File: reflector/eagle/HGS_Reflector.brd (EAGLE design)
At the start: 100 x 100 mm, 24 parts, among them J1 U.FL, U3 LP2985XX-N

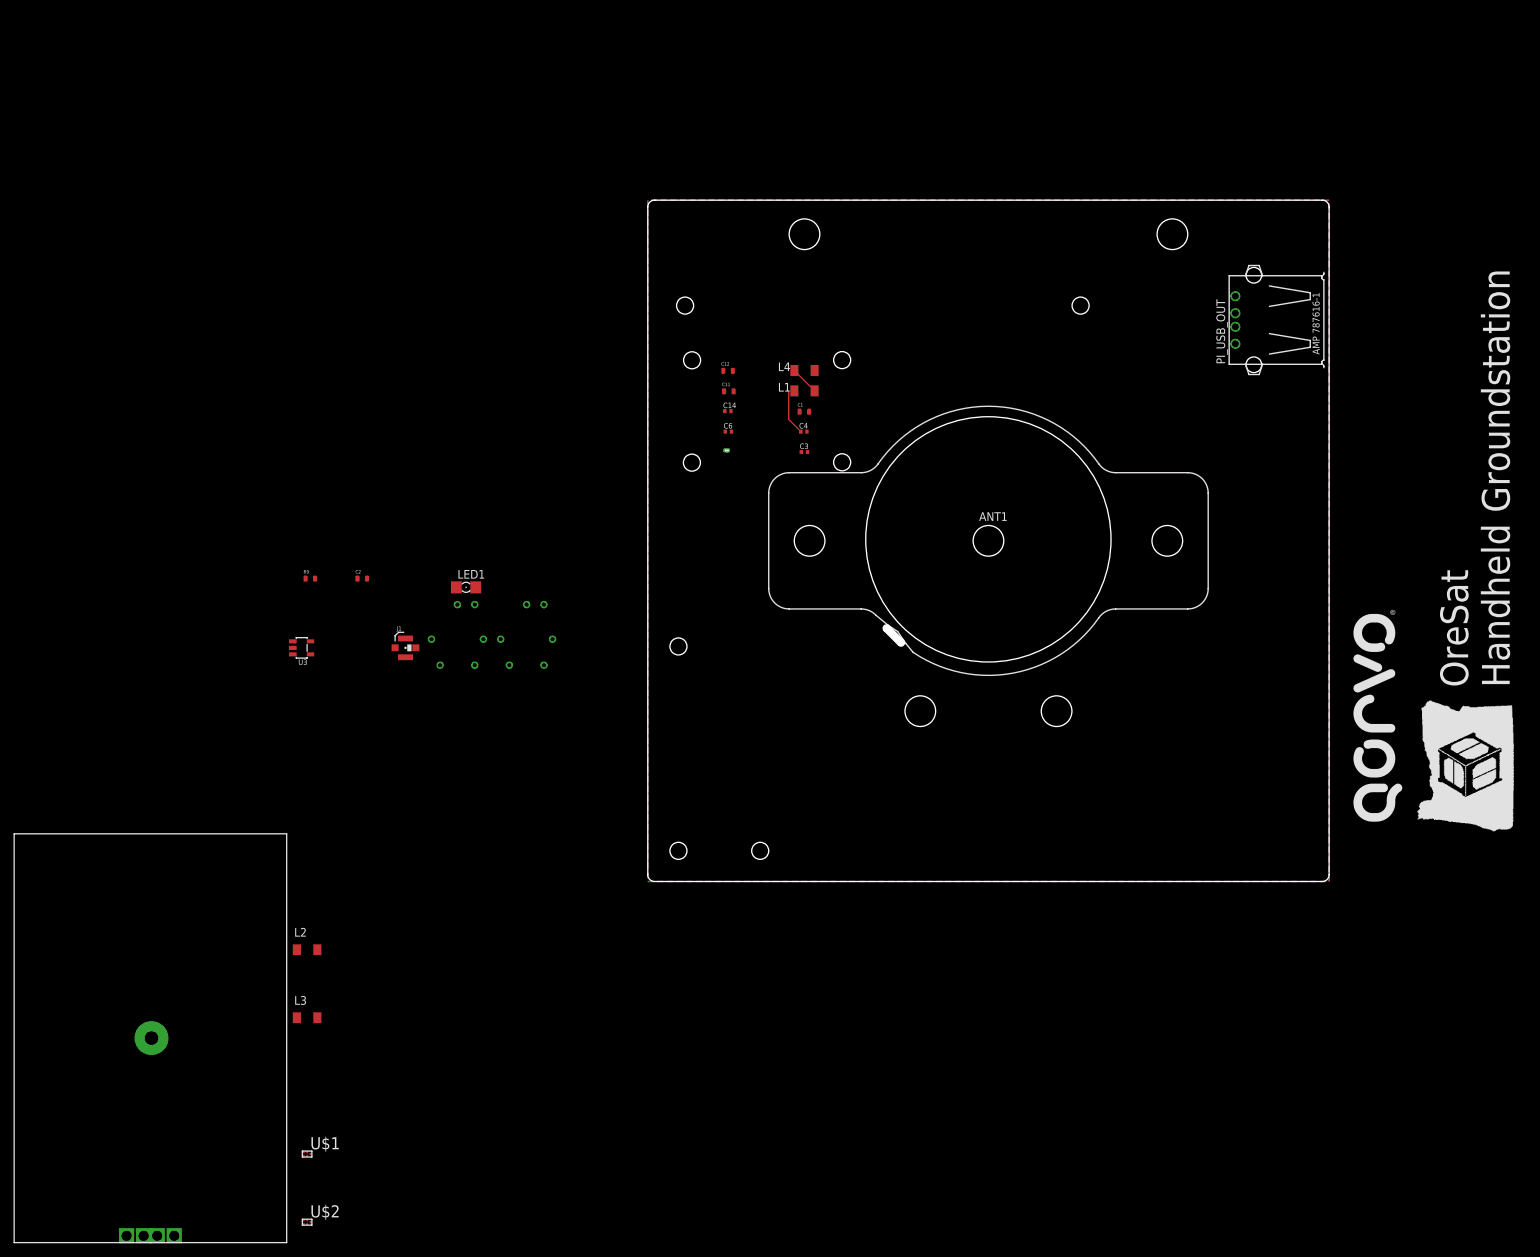
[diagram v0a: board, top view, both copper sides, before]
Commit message: I completed the physical layout of the board for HGS. Currently, I just need to sort through some DRC errors that I don't know how to fix, and do a design review.
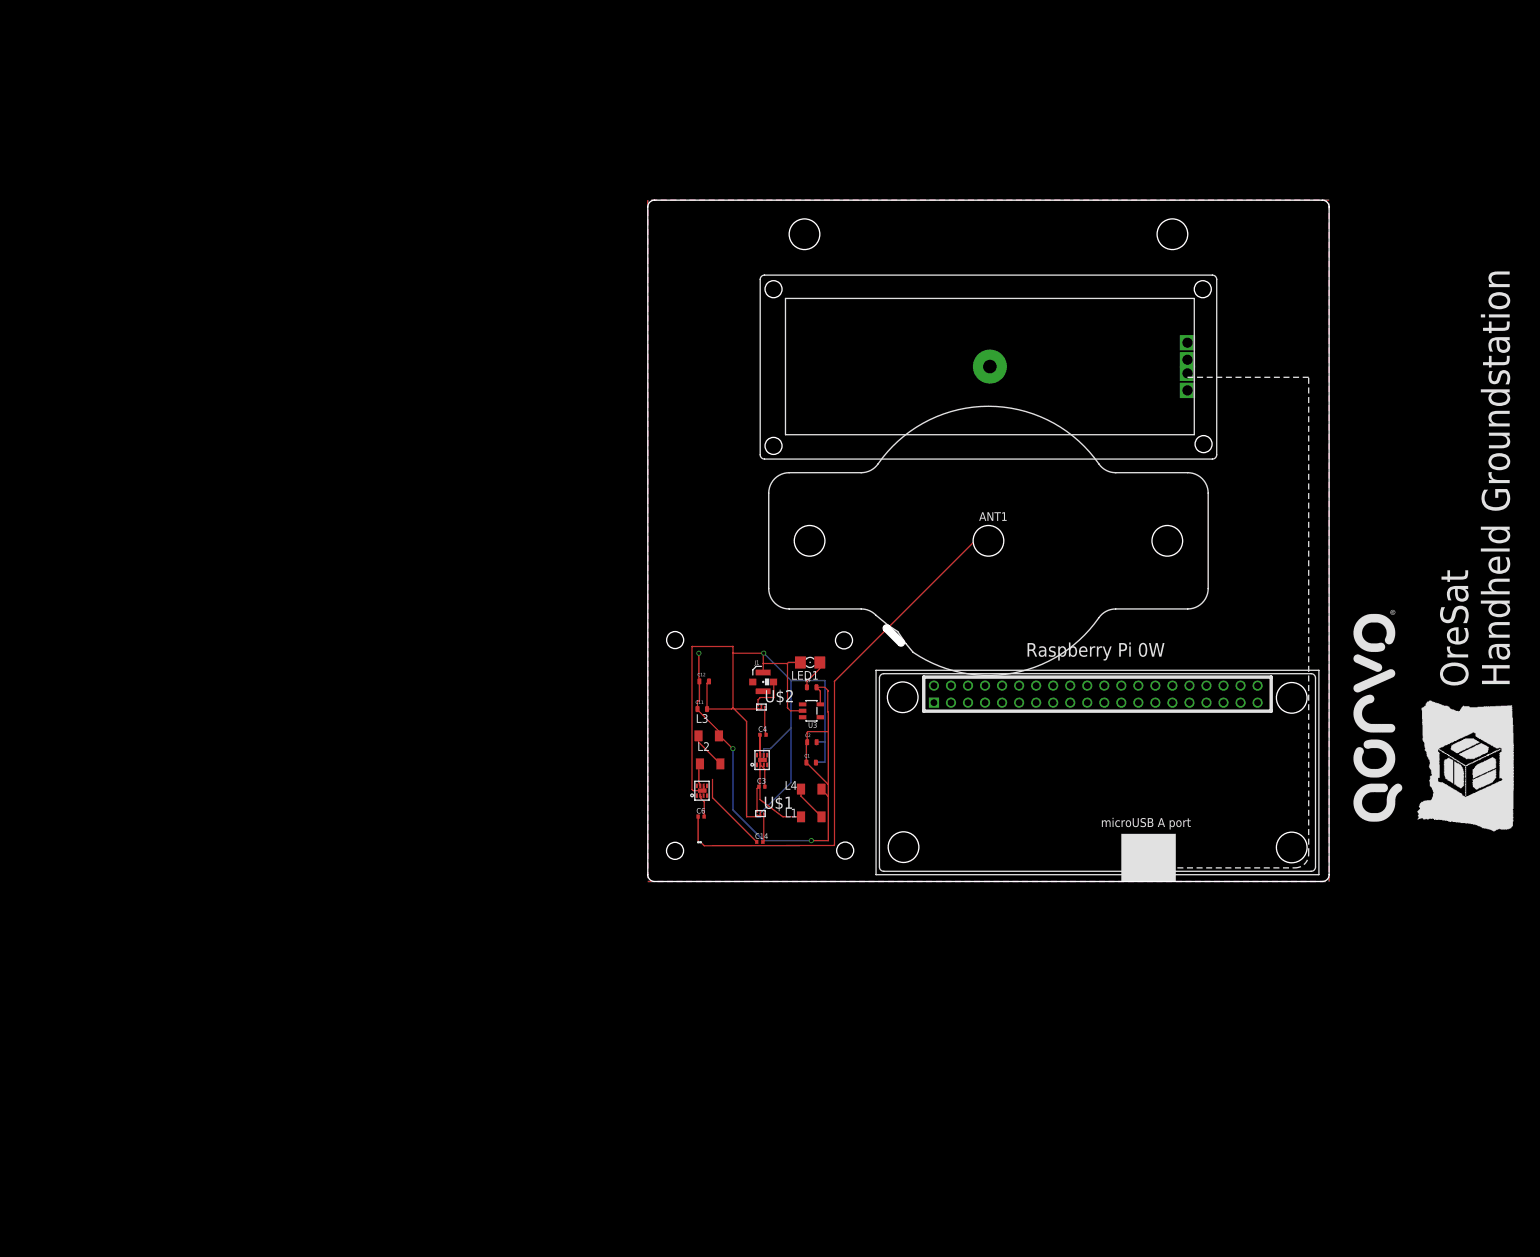
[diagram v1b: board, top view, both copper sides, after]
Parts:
- removed PI_USB_OUT: (no value), con-amp:USB
- added U$5: (no value), Rasp_Pi_0W:RASP_PI_0W
- U$6, U$7: device HGS_Data_Parts:TP3M9037 -> TP3M9037_LNA:TP3M9037
- moved U$4 157.8 mm to (50.2, 75.6), turned to 90 degrees
- moved U$2 100.8 mm to (16.7, 25.6)
- moved U$1 83.2 mm to (16.5, 9.97)
- moved U3 75.4 mm to (24.0, 25.1)
- moved R9 75.3 mm to (24.1, 28.5)
- moved L3 72.0 mm to (8.94, 21.4)
- moved C2 70.2 mm to (24.1, 20.4)
- moved L2 65.1 mm to (9.16, 17.3)
- moved C14 63.4 mm to (16.4, 5.81)
- moved L1 62.5 mm to (24.0, 9.50)
- moved L4 61.5 mm to (24.0, 13.6)
- moved U$3 57.6 mm to (7.59, 5.76), turned to 180 degrees
- moved C6 56.6 mm to (7.83, 9.53)
- moved J1 52.7 mm to (16.9, 29.3)
- moved LED1 51.7 mm to (23.8, 32.2), turned to 180 degrees
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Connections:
- removed net 3.3V1: L4.2
- removed net N$2: C4.1, U$6.RF_OUT
- net 1: no longer PI_USB_OUT.1
- net 3.3V: now also L4.2
- net GND: now also U$6.2X2_DFN_8PIN6, U$6.P$1, U$7.2X2_DFN_8PIN6, U$7.P$1; no longer U$6.GND, U$6.J7, U$6.SHTDN, U$6.VDD, U$7.GND, U$7.J7, U$7.SHTDN, U$7.VDD
- net N$11: now also U$7.2X2_DFN_8PIN2; no longer U$7.RF_IN
- net N$13: now also C4.1, U$6.2X2_DFN_8PIN7
- net N$16: now also U$7.2X2_DFN_8PIN7; no longer U$7.RF_OUT
- net N$18: no longer PI_USB_OUT.2
- net N$19: no longer PI_USB_OUT.3
- net N$8: now also U$6.2X2_DFN_8PIN2; no longer U$6.RF_IN
- net VCC: no longer PI_USB_OUT.4
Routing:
- net GND: track 0.00 -> 146.3 mm, vias 0 -> 1
- net 3.3V: track 0.00 -> 81.6 mm, vias 0 -> 3
- net N$12: track 0.00 -> 74.9 mm
- net N$13: track 0.00 -> 19.4 mm
- net N$16: track 0.00 -> 15.0 mm
- net N$2: track 6.71 -> 0.00 mm
- net N$5: track 0.00 -> 5.54 mm
- net N$7: track 0.00 -> 5.45 mm
- net N$10: track 0.00 -> 4.64 mm
- net N$6: track 0.00 -> 4.22 mm
- net N$3: track 0.00 -> 4.10 mm
- net N$9: track 0.00 -> 3.80 mm
- net N$4: track 0.00 -> 3.75 mm
- net N$8: track 0.00 -> 3.46 mm
- net N$11: track 0.00 -> 3.32 mm
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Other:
- board text removed: "Raspberry Pi Zero area"

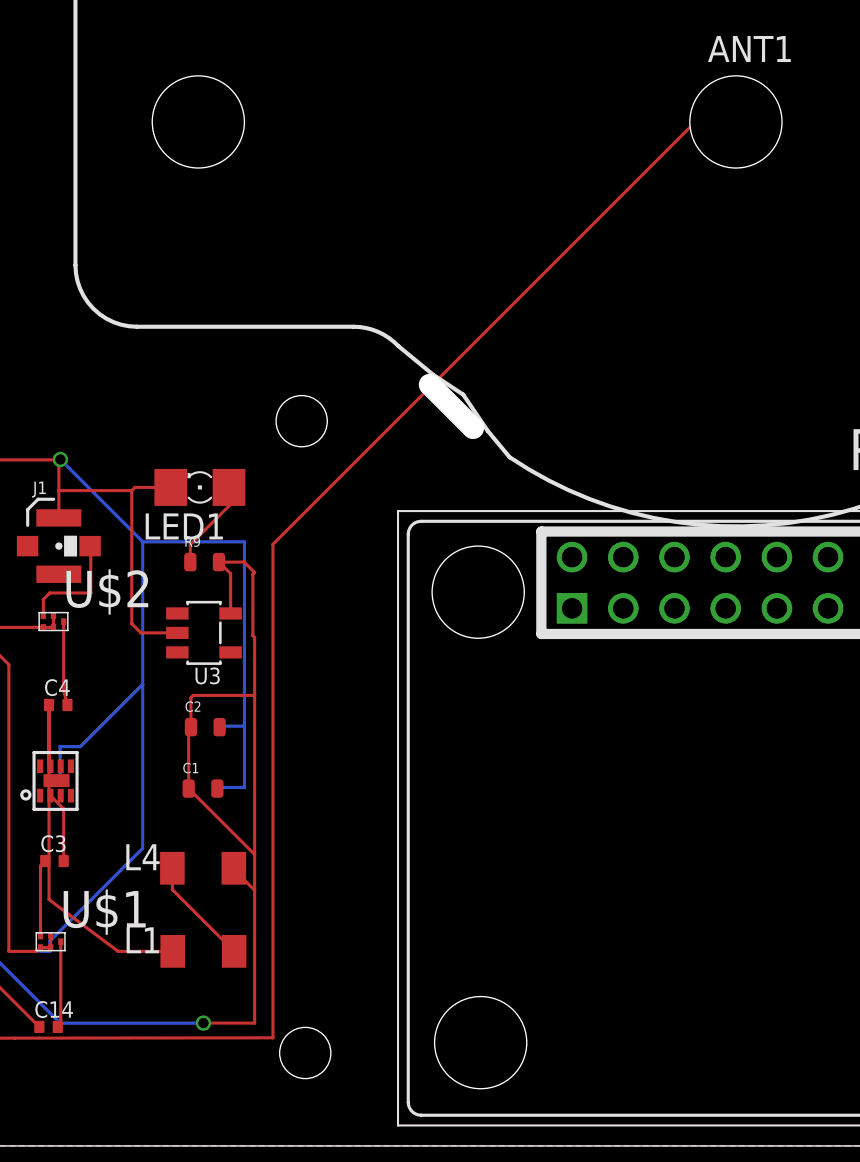
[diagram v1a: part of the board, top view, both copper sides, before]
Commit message: For the HGS board, I fixed some DRC clearance errors.
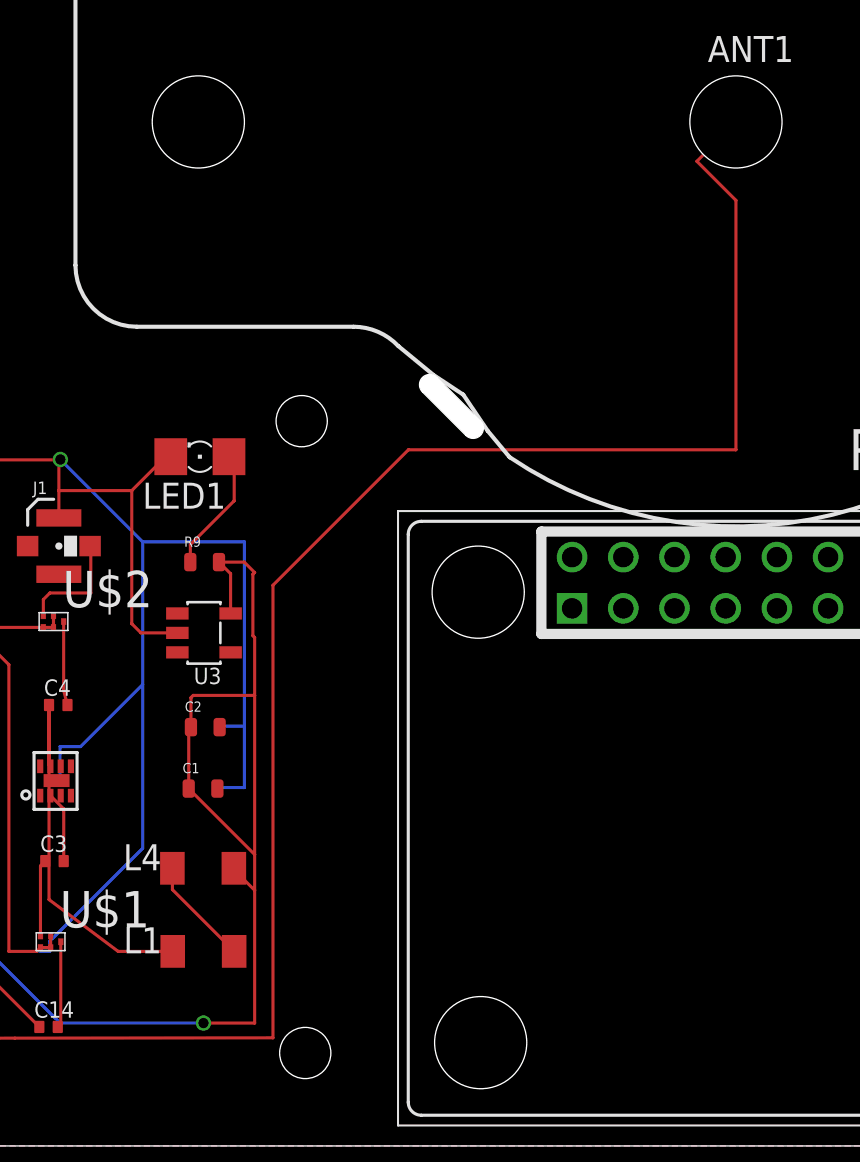
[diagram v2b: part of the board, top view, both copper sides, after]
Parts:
- moved LED1 1.50 mm to (23.8, 33.7)
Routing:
- net N$12: track 74.9 -> 84.7 mm
- net N$10: track 4.64 -> 6.14 mm
- net GND: track 146.3 -> 147.0 mm
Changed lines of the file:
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@@
 <wire x1="36.684640625" y1="36.684640625" x2="37.879190625" y2="34.91646875" width="0.2" layer="21"/>
 <wire x1="37.879190625" y1="34.91646875" x2="38.95165" y2="33.627159375" width="0.2" layer="21"/>
-<circle x="38.5" y="26.5" radius="3" width="0" layer="39" grouprefs="RASP_PI_DRILL"/>
 <circle x="77" y="95" radius="5.003996875" width="0" layer="39"/>
 <circle x="23" y="95" radius="5.003996875" width="0" layer="39"/>
@@
 <hole x="18.456828125" y="86.931990625" drill="2.5"/>
 <hole x="94.5129875" y="26.952734375" drill="4.5"/>
-<circle x="93.5" y="26.5" radius="3" width="0" layer="39"/>
 <hole x="37.536165625" y="5.044634375" drill="4.5"/>
-<circle x="38.5" y="6.5" radius="3" width="0" layer="39"/>
 <hole x="94.512790625" y="4.994334375" drill="4.5"/>
-<circle x="93.5" y="6.5" radius="3" width="0" layer="39"/>
 <wire x1="34" y1="29.865" x2="34.635" y2="30.5" width="0.1524" layer="21" curve="-90"/>
 <wire x1="34.635" y1="30.5" x2="97.365" y2="30.5" width="0.1524" layer="21"/>
@@
 <attribute name="VALUE" x="15.67" y="26.75" size="0.6096" layer="27" font="vector" ratio="20" align="top-left"/>
 </element>
-<element name="LED1" library="eagle-ltspice" library_urn="urn:adsk.eagle:library:217" package="LED_1206" package3d_urn="urn:adsk.eagle:package:13319/2" value="" x="23.825009375" y="32.154671875" smashed="yes" rot="R180">
-<attribute name="NAME" x="25.095009375" y="30.884671875" size="1.27" layer="25" rot="R180"/>
-<attribute name="SPICEMODEL" value="NONE" x="-2.844990625" y="75.334671875" size="1.778" layer="27" rot="R180" display="off"/>
-<attribute name="SPICEPREFIX" value="D" x="-2.844990625" y="75.334671875" size="1.778" layer="27" rot="R180" display="off"/>
-<attribute name="SPICETYPE" value="diode" x="-2.844990625" y="75.334671875" size="1.778" layer="27" rot="R180" display="off"/>
-<attribute name="VALUE" x="25.095009375" y="34.694671875" size="1.27" layer="27" rot="R180"/>
+<element name="LED1" library="eagle-ltspice" library_urn="urn:adsk.eagle:library:217" package="LED_1206" package3d_urn="urn:adsk.eagle:package:13319/2" value="" x="23.825009375" y="33.654671875" smashed="yes" rot="R180">
+<attribute name="NAME" x="25.095009375" y="32.384671875" size="1.27" layer="25" rot="R180"/>
+<attribute name="SPICEMODEL" value="NONE" x="-2.844990625" y="76.834671875" size="1.778" layer="27" rot="R180" display="off"/>
+<attribute name="SPICEPREFIX" value="D" x="-2.844990625" y="76.834671875" size="1.778" layer="27" rot="R180" display="off"/>
+<attribute name="SPICETYPE" value="diode" x="-2.844990625" y="76.834671875" size="1.778" layer="27" rot="R180" display="off"/>
+<attribute name="VALUE" x="25.095009375" y="36.194671875" size="1.27" layer="27" rot="R180"/>
 </element>
 <element name="R9" library="oresat-rcl" package=".0603-C-NOSILK" value="2K" x="24.057940625" y="28.5074125" smashed="yes">
@@
 <wire x1="20.5" y1="25.5" x2="20.5" y2="32" width="0.1524" layer="1"/>
 <wire x1="20.5" y1="32" x2="16.94" y2="32" width="0.1524" layer="1"/>
-<wire x1="20.5" y1="32" x2="20.654671875" y2="32.154671875" width="0.1524" layer="1"/>
-<wire x1="20.654671875" y1="32.154671875" x2="22.403009375" y2="32.154671875" width="0.1524" layer="1"/>
+<wire x1="20.5" y1="32" x2="22.154671875" y2="33.654671875" width="0.1524" layer="1"/>
+<wire x1="22.154671875" y1="33.654671875" x2="22.403009375" y2="33.654671875" width="0.1524" layer="1"/>
 <wire x1="12.5" y1="33.5" x2="12.5" y2="34.5" width="0.1524" layer="1"/>
 <wire x1="12.5" y1="34.5" x2="6.5" y2="34.5" width="0.1524" layer="1"/>
@@
 <wire x1="23.357940625" y1="28.5074125" x2="23.357940625" y2="29.357940625" width="0.1524" layer="1"/>
 <wire x1="23.357940625" y1="29.357940625" x2="25.5" y2="31.5" width="0.1524" layer="1"/>
-<wire x1="25.5" y1="31.5" x2="25.5" y2="31.90168125" width="0.1524" layer="1"/>
-<wire x1="25.5" y1="31.90168125" x2="25.247009375" y2="32.154671875" width="0.1524" layer="1"/>
+<wire x1="25.5" y1="31.5" x2="25.5" y2="33.40168125" width="0.1524" layer="1"/>
+<wire x1="25.5" y1="33.40168125" x2="25.247009375" y2="33.654671875" width="0.1524" layer="1"/>
 </signal>
 <signal name="3.3V">
@@
 <contactref element="ANT1" pad="1"/>
 <contactref element="U$3" pad="1"/>
-<wire x1="49.89391875" y1="49.877703125" x2="47.89391875" y2="49.877703125" width="0.1524" layer="1"/>
-<wire x1="47.89391875" y1="49.877703125" x2="27.39391875" y2="29.377703125" width="0.1524" layer="1"/>
-<wire x1="27.39391875" y1="29.377703125" x2="27.39391875" y2="5.2799125" width="0.1524" layer="1"/>
+<wire x1="49.89391875" y1="49.877703125" x2="48.093828125" y2="48.0776125" width="0.1524" layer="1"/>
+<wire x1="34.00810625" y1="33.991890625" x2="27.39391875" y2="27.377703125" width="0.1524" layer="1"/>
+<wire x1="27.39391875" y1="27.377703125" x2="27.39391875" y2="5.2799125" width="0.1524" layer="1"/>
 <wire x1="27.39391875" y1="5.2799125" x2="14.790690625" y2="5.2645375" width="0.1524" layer="1"/>
 <wire x1="14.790690625" y1="5.2645375" x2="8.279128125" y2="5.248671875" width="0.1524" layer="1"/>
 <wire x1="8.279128125" y1="5.248671875" x2="7.7932" y2="5.7346" width="0.1524" layer="1"/>
+<wire x1="34.00810625" y1="33.991890625" x2="49.991890625" y2="33.991890625" width="0.1524" layer="1"/>
+<wire x1="49.991890625" y1="33.991890625" x2="50" y2="34" width="0.1524" layer="1"/>
+<wire x1="50" y1="34" x2="50" y2="46.171440625" width="0.1524" layer="1"/>
+<wire x1="50" y1="46.171440625" x2="48.093828125" y2="48.0776125" width="0.1524" layer="1"/>
 </signal>
 <signal name="N$18">
